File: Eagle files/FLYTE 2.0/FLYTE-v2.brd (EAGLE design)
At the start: 100 x 80 mm, 56 parts, among them Q1 IRF540NPBF, Q2 IRF540NPBF, U2 XBP9B-XCST-021, U3 ADS1115IDGSR, U4 H3LIS200DLTR, U5 BS170F, U6 W25Q32JVSSIQ, U7 BS170F

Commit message: Delete extra BMP
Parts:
- removed U$2: BMP280, BMP280:BMP280
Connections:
- removed net 3.3V: U$2.SDO
- net 3V3: no longer U$2.VCC
- net GND: no longer U$2.GND
- net SCL: no longer U$2.SCL
- net SDA: no longer U$2.SDA
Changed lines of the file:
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@@
 </element>
 <element name="U$1" library="BMP280" package="BMP280" override_package3d_urn="urn:adsk.eagle:package:38477931/2" override_package_urn="urn:adsk.eagle:footprint:38477932/1" value="BMP280" x="-49.53" y="57.15" smashed="yes"/>
-<element name="U$2" library="BMP280" package="BMP280" override_package3d_urn="urn:adsk.eagle:package:38477931/2" override_package_urn="urn:adsk.eagle:footprint:38477932/1" value="BMP280" x="-66.04" y="57.15" smashed="yes"/>
 <element name="U$3" library="SDREADER" package="SDREADER" override_package3d_urn="urn:adsk.eagle:package:40384096/2" override_package_urn="urn:adsk.eagle:footprint:40384097/1" value="SDREADER" x="-33.02" y="57.15" smashed="yes"/>
 <element name="U$4" library="BNO055" package="BNO055" value="BNO055" x="-96.52" y="1.27" smashed="yes"/>
@@
 <contactref element="U6" pad="4"/>
 <contactref element="S1" pad="3"/>
-<contactref element="U$2" pad="GND"/>
 <contactref element="U$1" pad="SDO"/>
 <contactref element="U$4" pad="GND"/>
@@
 <wire x1="-27.69" y1="79.205" x2="-32.02" y2="71.85" width="0" layer="19" extent="1-1"/>
 <wire x1="-35.0012" y1="91.7194" x2="-27.69" y2="79.205" width="0" layer="19" extent="1-1"/>
-<wire x1="-62.23" y1="58.15" x2="-45.72" y2="58.15" width="0" layer="19" extent="1-1"/>
 <wire x1="-51.68" y1="92.71" x2="-35.0012" y2="91.7194" width="0" layer="19" extent="1-1"/>
 <wire x1="-51.68" y1="93.71" x2="-51.68" y2="92.71" width="0" layer="19" extent="1-1"/>
@@
 <contactref element="U1" pad="P$5"/>
 <contactref element="R4" pad="2"/>
-<contactref element="U$2" pad="SCL"/>
 <contactref element="U$4" pad="SCL"/>
 <contactref element="U3" pad="10"/>
@@
 <wire x1="-47.38" y1="93.71" x2="-29.16" y2="115.07" width="0" layer="19" extent="1-1"/>
 <wire x1="-43.18" y1="58.15" x2="-47.38" y2="93.71" width="0" layer="19" extent="1-1"/>
-<wire x1="-59.69" y1="58.15" x2="-43.18" y2="58.15" width="0" layer="19" extent="1-1"/>
 <wire x1="-35.4" y1="43.18" x2="-43.18" y2="58.15" width="0" layer="19" extent="1-1"/>
 <wire x1="-91.76" y1="102.87" x2="-47.38" y2="93.71" width="0" layer="19" extent="1-1"/>
-<wire x1="-81.915" y1="2.54" x2="-59.69" y2="58.15" width="0" layer="19" extent="1-1"/>
+<wire x1="-81.915" y1="2.54" x2="-35.4" y2="43.18" width="0" layer="19" extent="1-1"/>
 </signal>
 <signal name="SDA">
@@
 <contactref element="U1" pad="P$4"/>
 <contactref element="R3" pad="2"/>
-<contactref element="U$2" pad="SDA"/>
 <contactref element="U$4" pad="SDA"/>
 <contactref element="U3" pad="9"/>
@@
 <wire x1="-40.64" y1="58.15" x2="-47.38" y2="93.21" width="0" layer="19" extent="1-1"/>
 <wire x1="-35.4" y1="45.72" x2="-40.64" y2="58.15" width="0" layer="19" extent="1-1"/>
-<wire x1="-57.15" y1="58.15" x2="-40.64" y2="58.15" width="0" layer="19" extent="1-1"/>
-<wire x1="-79.375" y1="2.54" x2="-57.15" y2="58.15" width="0" layer="19" extent="1-1"/>
+<wire x1="-79.375" y1="2.54" x2="-35.4" y2="45.72" width="0" layer="19" extent="1-1"/>
 </signal>
 <signal name="3V3">
@@
 <contactref element="R17" pad="1"/>
 <contactref element="D1" pad="A"/>
-<contactref element="U$2" pad="VCC"/>
 <contactref element="U$4" pad="VIN"/>
 <contactref element="R22" pad="1"/>
@@
 <wire x1="-89.535" y1="2.54" x2="-93.17" y2="-46.03" width="0" layer="19" extent="1-1"/>
 <wire x1="-65.61" y1="26.53" x2="-89.535" y2="2.54" width="0" layer="19" extent="1-1"/>
-<wire x1="-64.77" y1="58.15" x2="-65.61" y2="26.53" width="0" layer="19" extent="1-1"/>
-<wire x1="-48.26" y1="58.15" x2="-64.77" y2="58.15" width="0" layer="19" extent="1-1"/>
+<wire x1="-48.26" y1="58.15" x2="-65.61" y2="26.53" width="0" layer="19" extent="1-1"/>
 <wire x1="-32.02" y1="59.15" x2="-48.26" y2="58.15" width="0" layer="19" extent="1-1"/>
-<wire x1="-81.28" y1="60.155" x2="-64.77" y2="58.15" width="0" layer="19" extent="1-1"/>
 <wire x1="-25.4" y1="79.205" x2="-32.02" y2="59.15" width="0" layer="19" extent="1-1"/>
 <wire x1="-33.58" y1="81.28" x2="-25.4" y2="79.205" width="0" layer="19" extent="1-1"/>
@@
 <wire x1="-85.46" y1="114.3" x2="-83.45" y2="114.3" width="0" layer="19" extent="1-1"/>
 <wire x1="-93.08" y1="114.3" x2="-85.46" y2="114.3" width="0" layer="19" extent="1-1"/>
+<wire x1="-81.28" y1="60.155" x2="-58.21" y2="80.645" width="0" layer="19" extent="1-1"/>
 </signal>
 <signal name="TX">
@@
 <wire x1="-35.4" y1="50.8" x2="-91.17" y2="-35.87" width="0" layer="19" extent="1-1"/>
 </signal>
-<signal name="3.3V">
-<contactref element="U$2" pad="SDO"/>
-</signal>
 <signal name="BNO_INT">

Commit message: Improve pyros
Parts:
- removed BATTERY, DROGUE, MAIN: XT30UPB-M, XT30UPB-M:XT30UPB-M
- removed MA_ARM: (no value), con-wago-500:W237-102
- removed Q1, Q2: IRF540NPBF, IRF540NPBF:TO254P1054X469X1930-3
- removed R24, R26: 100K ohm, rcl:R0805
- added DROGUE_PYRO, J1, MAIN_PYRO: XT30PW-M, XT30PW-M:AMASS_XT30PW-M
- added MAIN_ARM: (no value), con-wago-500:W237-102
- added R6: 4.7K, rcl:R0805
- added R7: 10 ohm, rcl:0207/10
- R11, R12: value 10 ohm -> 100K ohm; device rcl:0207/10 -> rcl:R0805
- R8: value 4.7K -> 10 ohm; device rcl:R0805 -> rcl:0207/10
- moved R8 249.9 mm to (-105.4, -137.2)
- moved R12 246.2 mm to (-109.2, -129.5)
- moved R11 236.6 mm to (-99.1, -119.4)
- moved U7 83.8 mm to (-91.4, -101.6)
- renumbered 3.3V_REGULATOR to BATTERY_REGULATOR3V3, 3.3V_REGULATOR1 to USB_REGULATOR3V3
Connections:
- removed net N$13: Q1.2, R11.2, R12.2, R24.1, U7.3
- removed net N$14: MAIN.P$2, MA_ARM.1
- new net N$4: MAIN_PYRO.N, R7.1, R8.1
- new net N$5: R11.1, R7.2, R8.2, U7.3
- net 3V3: now also SERIAL.4
- net DROGUE: now also R1.2; no longer Q2.1, R1.1
- net GND: now also GPS.3, J1.N, R1.1, R12.2, R6.1; no longer BATTERY.P$2, GPS.1, Q1.3, Q2.3, R1.2, R26.2, R8.2
- net MAIN: now also R6.2; no longer Q1.1, R8.1
- net N$12: no longer Q2.2
- net N$2: now also DROGUE_PYRO.P, DR_ARM.2; no longer DROGUE.P$2, DR_ARM.1
- net N$6: now also MAIN_ARM.2, MAIN_PYRO.P; no longer MAIN.P$1, R11.1, R12.1
- net N$7: now also DROGUE_PYRO.N; no longer DROGUE.P$1
- net RX: now also GPS.1; no longer GPS.3
- net SENSE_DROG: now also R23.2, R25.1; no longer R24.2, R26.1
- net SENSE_MAIN: now also R11.2, R12.1; no longer R23.2, R25.1
- net VCC: now also DR_ARM.1, J1.P, MAIN_ARM.1; no longer BATTERY.P$1, DR_ARM.2, MA_ARM.2

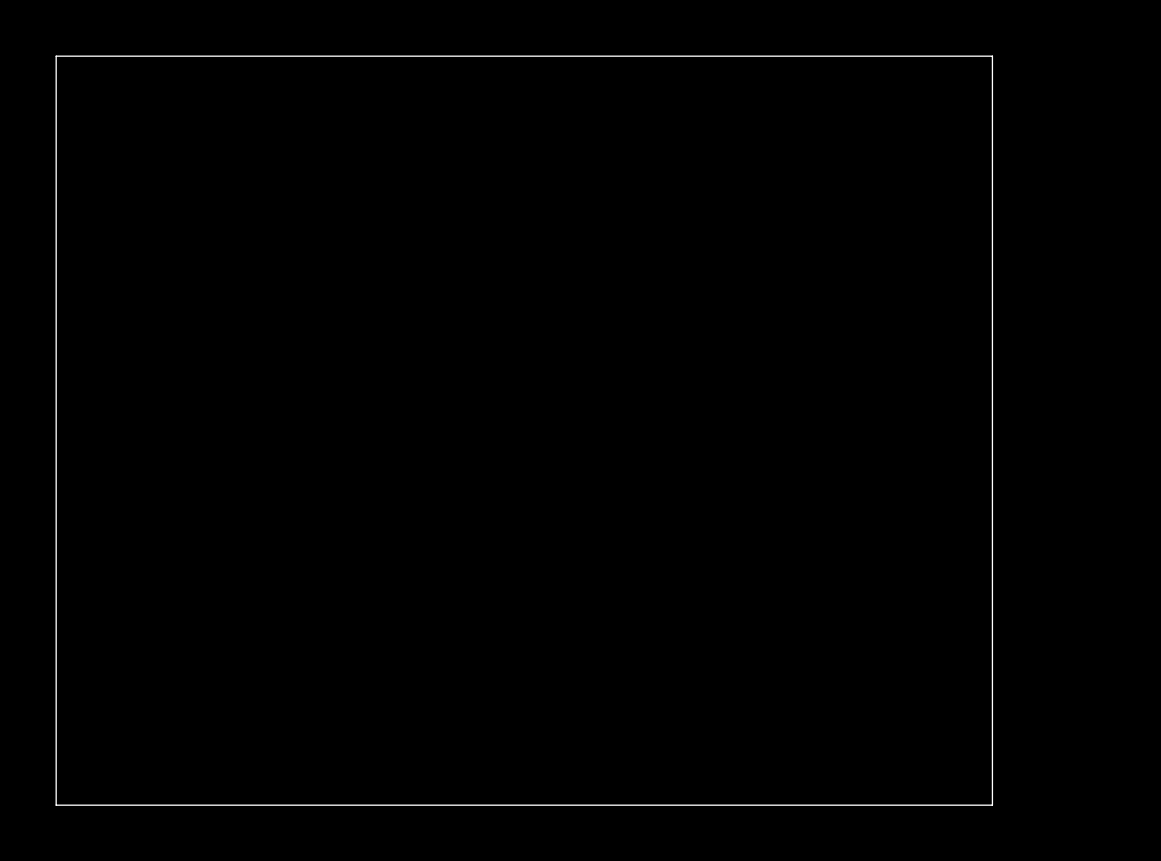
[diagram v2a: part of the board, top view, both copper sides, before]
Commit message: Cleanup main board and add motor controller
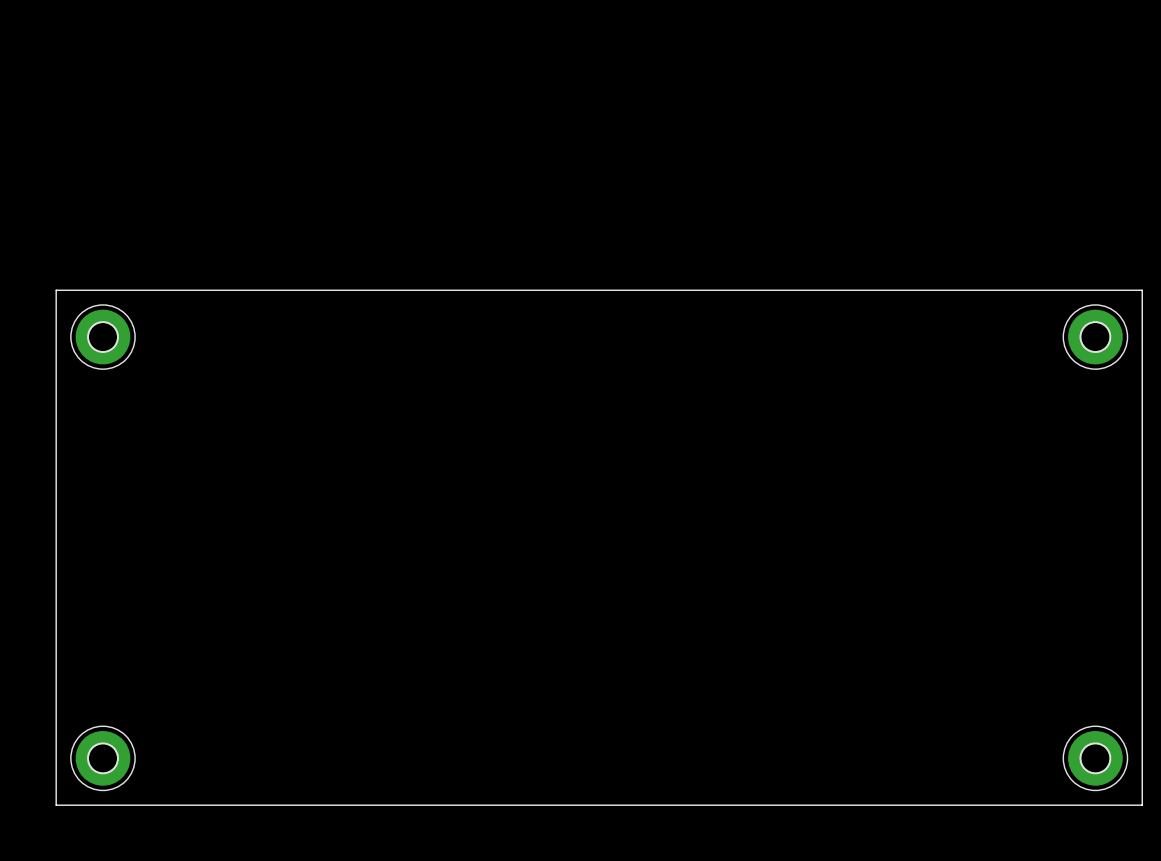
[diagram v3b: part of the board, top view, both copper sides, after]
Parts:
- added H1, H2, H3, H4: MOUNT-PAD-ROUND3.0, holes:3,0-PAD
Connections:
- net MISO_0 renamed MISO0
- net MISO_1 renamed MISO1
- net MOSI_0 renamed MOSI0
- net MOSI_1 renamed MOSI1
- net SCK_0 renamed SCK0
- net SCK_1 renamed SCK1
- net SCL renamed SCL1
- removed net SDA: R3.2, U$1.SDA, U$4.SDA, U1.P$4, U3.9, U4.6
- new net AIR_DATA: U1.P$34
- new net AIR_SCK: U1.P$32
- net GND: now also H1.B3,0, H2.B3,0, H3.B3,0, H4.B3,0
- net SCL0: now also R5.2
- net SDA1: now also R3.2, U$1.SDA, U$4.SDA, U1.P$4, U3.9, U4.6; no longer R5.2
- net SENSE_DROG: no longer U1.P$32
- net SENSE_MAIN: no longer U1.P$34
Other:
- board size 100 x 80 mm -> 116 x 55 mm
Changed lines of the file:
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@@
 <setting verticaltext="up"/>
 </settings>
-<grid distance="50" unitdist="mil" unit="mil" style="lines" multiple="1" display="no" altdistance="5" altunitdist="mil" altunit="mil"/>
+<grid distance="50" unitdist="mil" unit="mm" style="lines" multiple="1" display="no" altdistance="5" altunitdist="mil" altunit="mm"/>
 <layers>
 <layer number="1" name="Top" color="4" fill="1" visible="yes" active="yes"/>
@@
 <layer number="43" name="vRestrict" color="2" fill="10" visible="yes" active="yes"/>
 <layer number="44" name="Drills" color="7" fill="1" visible="no" active="yes"/>
-<layer number="45" name="Holes" color="7" fill="1" visible="no" active="yes"/>
+<layer number="45" name="Holes" color="7" fill="1" visible="yes" active="yes"/>
 <layer number="46" name="Milling" color="3" fill="1" visible="no" active="yes"/>
 <layer number="47" name="Measures" color="7" fill="1" visible="no" active="yes"/>
@@
 <board>
 <plain>
-<wire x1="0" y1="0" x2="100" y2="0" width="0" layer="20"/>
-<wire x1="100" y1="0" x2="100" y2="80" width="0" layer="20"/>
-<wire x1="100" y1="80" x2="0" y2="80" width="0" layer="20"/>
-<wire x1="0" y1="80" x2="0" y2="0" width="0" layer="20"/>
+<wire x1="0" y1="0" x2="116" y2="0" width="0" layer="20"/>
+<wire x1="116" y1="0" x2="116" y2="55" width="0" layer="20"/>
+<wire x1="116" y1="55" x2="0" y2="55" width="0" layer="20"/>
+<wire x1="0" y1="55" x2="0" y2="0" width="0" layer="20"/>
 </plain>
 <attributes>
@@
 <attribute name="VALUE" x="-111.76" y="-115.57" size="1.27" layer="27"/>
 </element>
+<element name="H1" library="holes" library_urn="urn:adsk.eagle:library:237" package="3,0-PAD" package3d_urn="urn:adsk.eagle:package:14280/1" value="MOUNT-PAD-ROUND3.0" x="5" y="5" smashed="yes">
+<attribute name="POPULARITY" value="17" x="5" y="5" size="1.778" layer="27" display="off"/>
+</element>
+<element name="H2" library="holes" library_urn="urn:adsk.eagle:library:237" package="3,0-PAD" package3d_urn="urn:adsk.eagle:package:14280/1" value="MOUNT-PAD-ROUND3.0" x="5" y="50" smashed="yes">
+<attribute name="POPULARITY" value="17" x="5" y="50" size="1.778" layer="27" display="off"/>
+</element>
+<element name="H3" library="holes" library_urn="urn:adsk.eagle:library:237" package="3,0-PAD" package3d_urn="urn:adsk.eagle:package:14280/1" value="MOUNT-PAD-ROUND3.0" x="111" y="5" smashed="yes">
+<attribute name="POPULARITY" value="17" x="111" y="5" size="1.778" layer="27" display="off"/>
+</element>
+<element name="H4" library="holes" library_urn="urn:adsk.eagle:library:237" package="3,0-PAD" package3d_urn="urn:adsk.eagle:package:14280/1" value="MOUNT-PAD-ROUND3.0" x="111" y="50" smashed="yes">
+<attribute name="POPULARITY" value="17" x="111" y="50" size="1.778" layer="27" display="off"/>
+</element>
 </elements>
 <signals>
@@
 <contactref element="R6" pad="1"/>
 <contactref element="GPS" pad="3"/>
+<contactref element="H1" pad="B3,0"/>
+<contactref element="H2" pad="B3,0"/>
+<contactref element="H3" pad="B3,0"/>
+<contactref element="H4" pad="B3,0"/>
 <wire x1="-100.01" y1="-129.54" x2="-108.27" y2="-129.54" width="0" layer="19" extent="1-1"/>
 <wire x1="-92.456" y1="-102.5144" x2="-100.01" y2="-129.54" width="0" layer="19" extent="1-1"/>
@@
 <wire x1="-15.4" y1="22.86" x2="-15.4" y2="35.56" width="0" layer="19" extent="1-1"/>
 <wire x1="-15.4" y1="10.16" x2="-15.4" y2="22.86" width="0" layer="19" extent="1-1"/>
+<wire x1="5" y1="50" x2="-15.4" y2="48.26" width="0" layer="19" extent="1-1"/>
+<wire x1="5" y1="5" x2="-15.4" y2="10.16" width="0" layer="19" extent="1-1"/>
 <wire x1="-29.16" y1="114.57" x2="-35.0012" y2="91.7194" width="0" layer="19" extent="1-1"/>
 <wire x1="-27.94" y1="114.35" x2="-29.16" y2="114.57" width="0" layer="19" extent="1-1"/>
@@
 <wire x1="-94.88" y1="114.3" x2="-91.07" y2="114.3" width="0" layer="19" extent="1-1"/>
 <wire x1="-83.57" y1="60.155" x2="-58.21" y2="79.375" width="0" layer="19" extent="1-1"/>
+<wire x1="111" y1="50" x2="5" y2="50" width="0" layer="19" extent="1-1"/>
+<wire x1="111" y1="5" x2="111" y2="50" width="0" layer="19" extent="1-1"/>
 </signal>
 <signal name="VCC">
@@
 <wire x1="-23.11" y1="79.205" x2="-47.38" y2="92.21" width="0" layer="19" extent="1-1"/>
 </signal>
-<signal name="SCL">
+<signal name="SCL1">
 <contactref element="U$1" pad="SCL"/>
 <contactref element="U1" pad="P$5"/>
@@
 <wire x1="-91.76" y1="102.87" x2="-47.38" y2="93.71" width="0" layer="19" extent="1-1"/>
 <wire x1="-81.915" y1="2.54" x2="-35.4" y2="43.18" width="0" layer="19" extent="1-1"/>
-</signal>
-<signal name="SDA">
-<contactref element="U$1" pad="SDA"/>
-<contactref element="U1" pad="P$4"/>
-<contactref element="R3" pad="2"/>
-<contactref element="U$4" pad="SDA"/>
-<contactref element="U3" pad="9"/>
-<contactref element="U4" pad="6"/>
-<wire x1="-47.38" y1="93.21" x2="-28.44" y2="114.35" width="0" layer="19" extent="1-1"/>
-<wire x1="-81.6" y1="102.87" x2="-47.38" y2="93.21" width="0" layer="19" extent="1-1"/>
-<wire x1="-40.64" y1="58.15" x2="-47.38" y2="93.21" width="0" layer="19" extent="1-1"/>
-<wire x1="-35.4" y1="45.72" x2="-40.64" y2="58.15" width="0" layer="19" extent="1-1"/>
-<wire x1="-79.375" y1="2.54" x2="-35.4" y2="45.72" width="0" layer="19" extent="1-1"/>
 </signal>
 <signal name="3V3">
@@
 <wire x1="-15.4" y1="17.78" x2="-92.456" y2="-100.6856" width="0" layer="19" extent="1-1"/>
 </signal>
-<signal name="MISO_1">
+<signal name="MISO1">
 <contactref element="U$3" pad="MISO"/>
 <contactref element="U1" pad="P$16"/>
@@
 <wire x1="-35.4" y1="15.24" x2="-32.02" y2="69.31" width="0" layer="19" extent="1-1"/>
 </signal>
-<signal name="SCK_1">
+<signal name="SCK1">
 <contactref element="U$3" pad="CLK"/>
 <contactref element="U1" pad="P$14"/>
@@
 <wire x1="-35.4" y1="20.32" x2="-32.02" y2="66.77" width="0" layer="19" extent="1-1"/>
 </signal>
-<signal name="MOSI_1">
+<signal name="MOSI1">
 <contactref element="U$3" pad="MOSI"/>
 <contactref element="U1" pad="P$15"/>
@@
 <wire x1="-35.4" y1="17.78" x2="-32.02" y2="64.23" width="0" layer="19" extent="1-1"/>
 </signal>
-<signal name="MOSI_0">
+<signal name="MOSI0">
 <contactref element="U1" pad="P$25"/>
 <contactref element="U2" pad="11"/>
 <wire x1="-15.4" y1="15.24" x2="-43.61" y2="8.53" width="0" layer="19" extent="1-1"/>
 </signal>
-<signal name="SCK_0">
+<signal name="SCK0">
 <contactref element="U1" pad="P$24"/>
 <contactref element="U2" pad="18"/>
 <wire x1="-15.4" y1="12.7" x2="-43.61" y2="22.53" width="0" layer="19" extent="1-1"/>
 </signal>
-<signal name="MISO_0">
+<signal name="MISO0">
 <contactref element="U1" pad="P$21"/>
 <contactref element="R16" pad="1"/>
@@
 <signal name="SENSE_MAIN">
 <contactref element="U3" pad="4"/>
-<contactref element="U1" pad="P$34"/>
 <contactref element="R11" pad="2"/>
 <contactref element="R12" pad="1"/>
 <wire x1="-98.11" y1="-119.38" x2="-110.17" y2="-129.54" width="0" layer="19" extent="1-1"/>
-<wire x1="-15.4" y1="38.1" x2="-98.11" y2="-119.38" width="0" layer="19" extent="1-1"/>
-<wire x1="-51.68" y1="92.21" x2="-15.4" y2="38.1" width="0" layer="19" extent="1-1"/>
+<wire x1="-51.68" y1="92.21" x2="-98.11" y2="-119.38" width="0" layer="19" extent="1-1"/>
 </signal>
 <signal name="SDA0">
@@
 <contactref element="U1" pad="P$7"/>
 <contactref element="MOTOR" pad="3"/>
+<contactref element="R5" pad="2"/>
+<wire x1="-91.17" y1="-56.19" x2="-94.3" y2="-72.39" width="0" layer="19" extent="1-1"/>
 <wire x1="-35.4" y1="38.1" x2="-91.17" y2="-56.19" width="0" layer="19" extent="1-1"/>
 </signal>
@@
 </signal>
 <signal name="SENSE_DROG">
-<contactref element="U1" pad="P$32"/>
 <contactref element="U3" pad="5"/>
 <contactref element="R23" pad="2"/>
@@
 <wire x1="-53.02" y1="102.87" x2="-30.8" y2="102.87" width="0" layer="19" extent="1-1"/>
 <wire x1="-51.68" y1="91.71" x2="-53.02" y2="102.87" width="0" layer="19" extent="1-1"/>
-<wire x1="-15.4" y1="33.02" x2="-51.68" y2="91.71" width="0" layer="19" extent="1-1"/>
 </signal>
 <signal name="N$17">
@@
 </signal>
 <signal name="SDA1">
-<contactref element="R5" pad="2"/>
+<contactref element="U$1" pad="SDA"/>
+<contactref element="U1" pad="P$4"/>
+<contactref element="R3" pad="2"/>
+<contactref element="U$4" pad="SDA"/>
+<contactref element="U3" pad="9"/>
+<contactref element="U4" pad="6"/>
+<wire x1="-47.38" y1="93.21" x2="-28.44" y2="114.35" width="0" layer="19" extent="1-1"/>
+<wire x1="-81.6" y1="102.87" x2="-47.38" y2="93.21" width="0" layer="19" extent="1-1"/>
+<wire x1="-40.64" y1="58.15" x2="-47.38" y2="93.21" width="0" layer="19" extent="1-1"/>
+<wire x1="-35.4" y1="45.72" x2="-40.64" y2="58.15" width="0" layer="19" extent="1-1"/>
+<wire x1="-79.375" y1="2.54" x2="-35.4" y2="45.72" width="0" layer="19" extent="1-1"/>
 </signal>
 <signal name="N$4">
@@
 <wire x1="-107.91" y1="-109.06" x2="-104.18" y2="-121.92" width="0" layer="19" extent="1-1"/>
 </signal>
+<signal name="AIR_DATA">
+<contactref element="U1" pad="P$34"/>
+</signal>
+<signal name="AIR_SCK">
+<contactref element="U1" pad="P$32"/>
+</signal>
 </signals>

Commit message: Start layout
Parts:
- removed J1: XT30PW-M, XT30PW-M:AMASS_XT30PW-M
- added JP2: (no value), pinhead:1X04
- added POWER: XT30PW-M, XT30PW-M:AMASS_XT30PW-M
- moved MAIN_ARM 269.7 mm to (100.5, 52.0)
- moved R8 267.8 mm to (96.7, 38.6), turned to 90 degrees
- moved R12 264.8 mm to (93.7, 40.5), flipped to the bottom
- moved MAIN_PYRO 258.2 mm to (114.0, 37.0), turned to 270 degrees
- moved R6 254.6 mm to (93.9, 36.5), flipped to the bottom, turned to 180 degrees
- moved R11 254.6 mm to (99.1, 40.5), flipped to the bottom
- moved R7 252.9 mm to (100.0, 38.6), turned to 90 degrees
- moved U7 236.0 mm to (99.6, 37.1), flipped to the bottom, turned to 180 degrees
- moved R5 218.2 mm to (89.0, 44.6), turned to 180 degrees
- moved R2 211.0 mm to (85.0, 43.7), turned to 90 degrees
- moved MOTOR 210.2 mm to (87.0, 53.5), turned to 180 degrees
- moved U$4 193.0 mm to (94.5, 28.7), turned to 180 degrees
- moved GPS 191.3 mm to (71.0, 53.5), turned to 180 degrees
- moved C7 187.4 mm to (85.1, 30.6), flipped to the bottom, turned to 180 degrees
- moved R4 178.7 mm to (75.0, 41.3), flipped to the bottom, turned to 90 degrees
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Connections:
- net 3V3: now also JP2.4
- net AIR_DATA: now also JP2.3
- net AIR_SCK: now also JP2.2
- net GND: now also JP2.1, POWER.N; no longer J1.N
- net N$2: now also DROGUE_PYRO.N, DR_ARM.1; no longer DROGUE_PYRO.P, DR_ARM.2
- net N$7: now also DROGUE_PYRO.P; no longer DROGUE_PYRO.N
- net VCC: now also DR_ARM.2, POWER.P; no longer DR_ARM.1, J1.P
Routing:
- net 3V3: track 0.00 -> 252.7 mm, vias 0 -> 1
- net VCC: track 0.00 -> 98.3 mm
- net MISO1: track 0.00 -> 44.4 mm, vias 0 -> 1
- net MOSI1: track 0.00 -> 39.6 mm
- net SCK1: track 0.00 -> 38.2 mm
- net CS_SD: track 0.00 -> 34.8 mm
- net SCL0: track 0.00 -> 28.2 mm, vias 0 -> 1
- net SDA1: track 0.00 -> 27.3 mm
- net SDA0: track 0.00 -> 23.7 mm, vias 0 -> 1
- net SCL1: track 0.00 -> 22.4 mm
- net SER_TX: track 0.00 -> 21.5 mm, vias 0 -> 1
- net SER_RX: track 0.00 -> 18.3 mm, vias 0 -> 1
- net BUZZER: track 0.00 -> 18.1 mm, vias 0 -> 1
- net N$2: track 0.00 -> 11.7 mm
- net N$6: track 0.00 -> 11.6 mm
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- added copper zone on layer 1, net GND
- added copper zone on layer 16, net GND
